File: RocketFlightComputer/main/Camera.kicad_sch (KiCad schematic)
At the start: 1 part

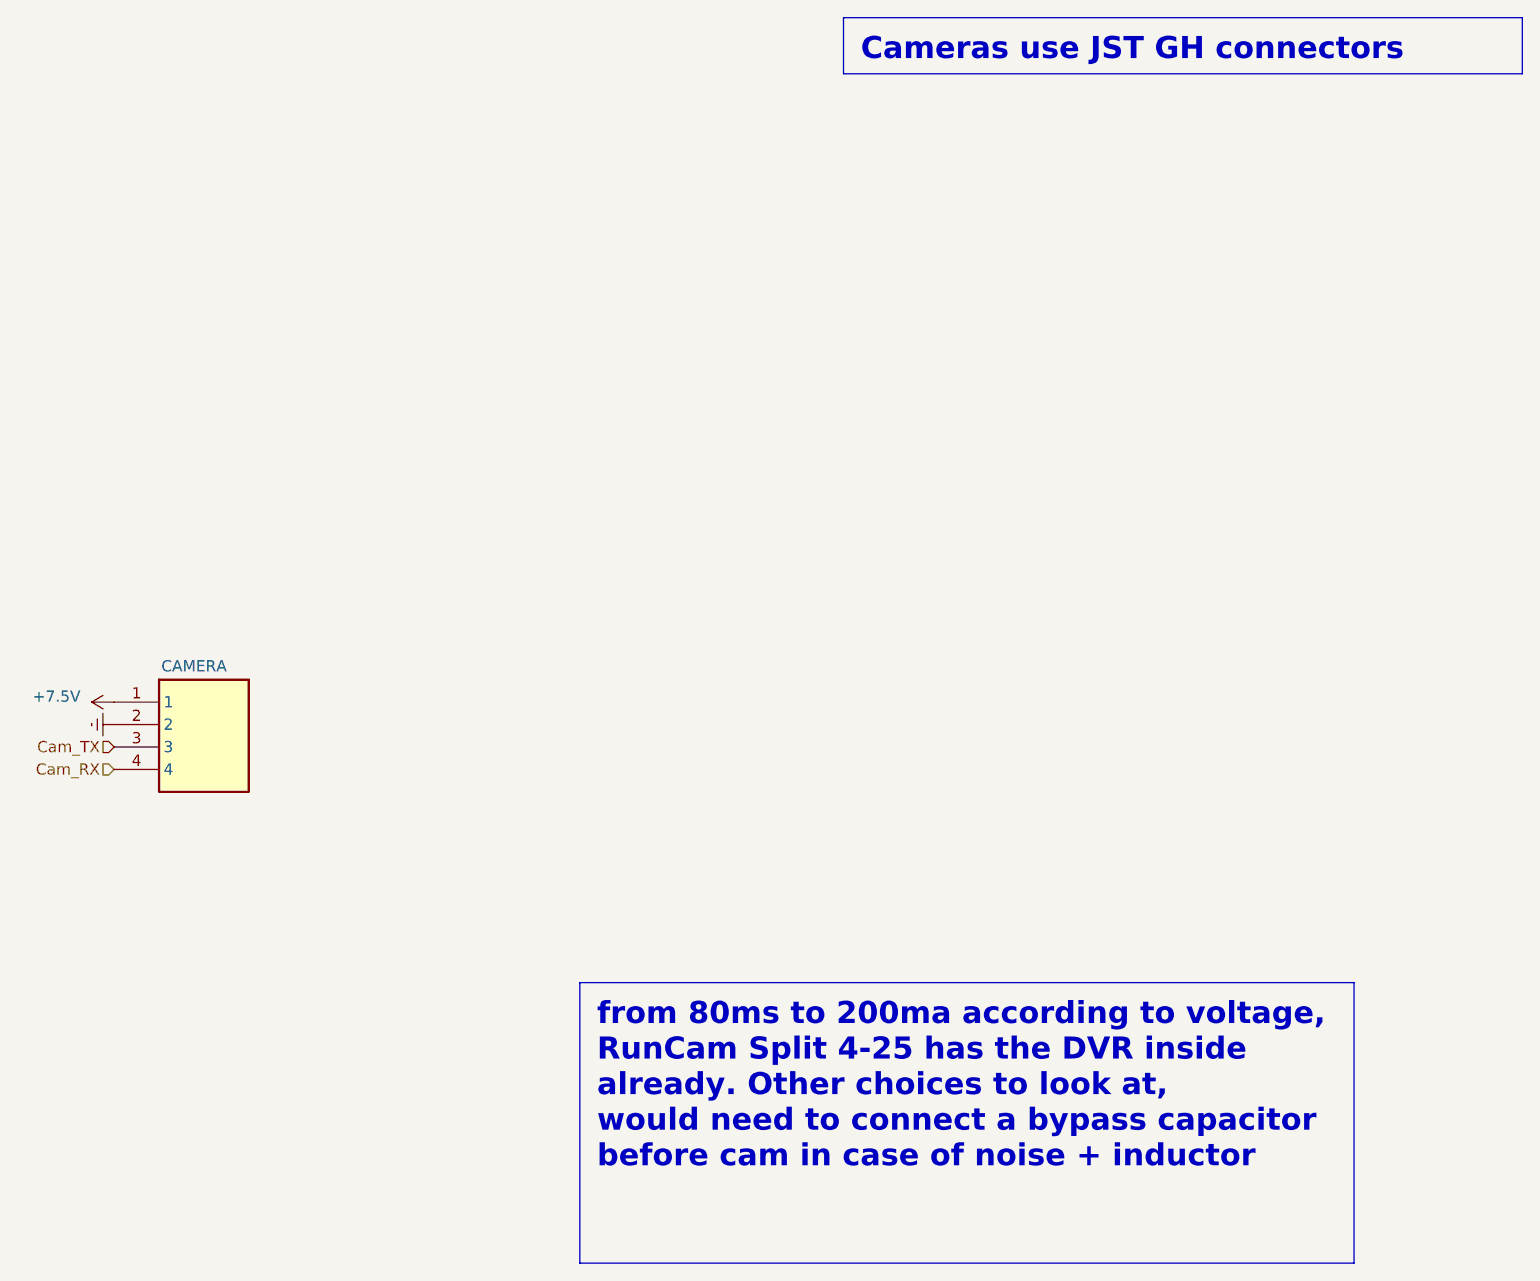
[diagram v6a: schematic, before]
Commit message: Change of winbond flash to other one supported by teensy bootloader since winbond is out of stock
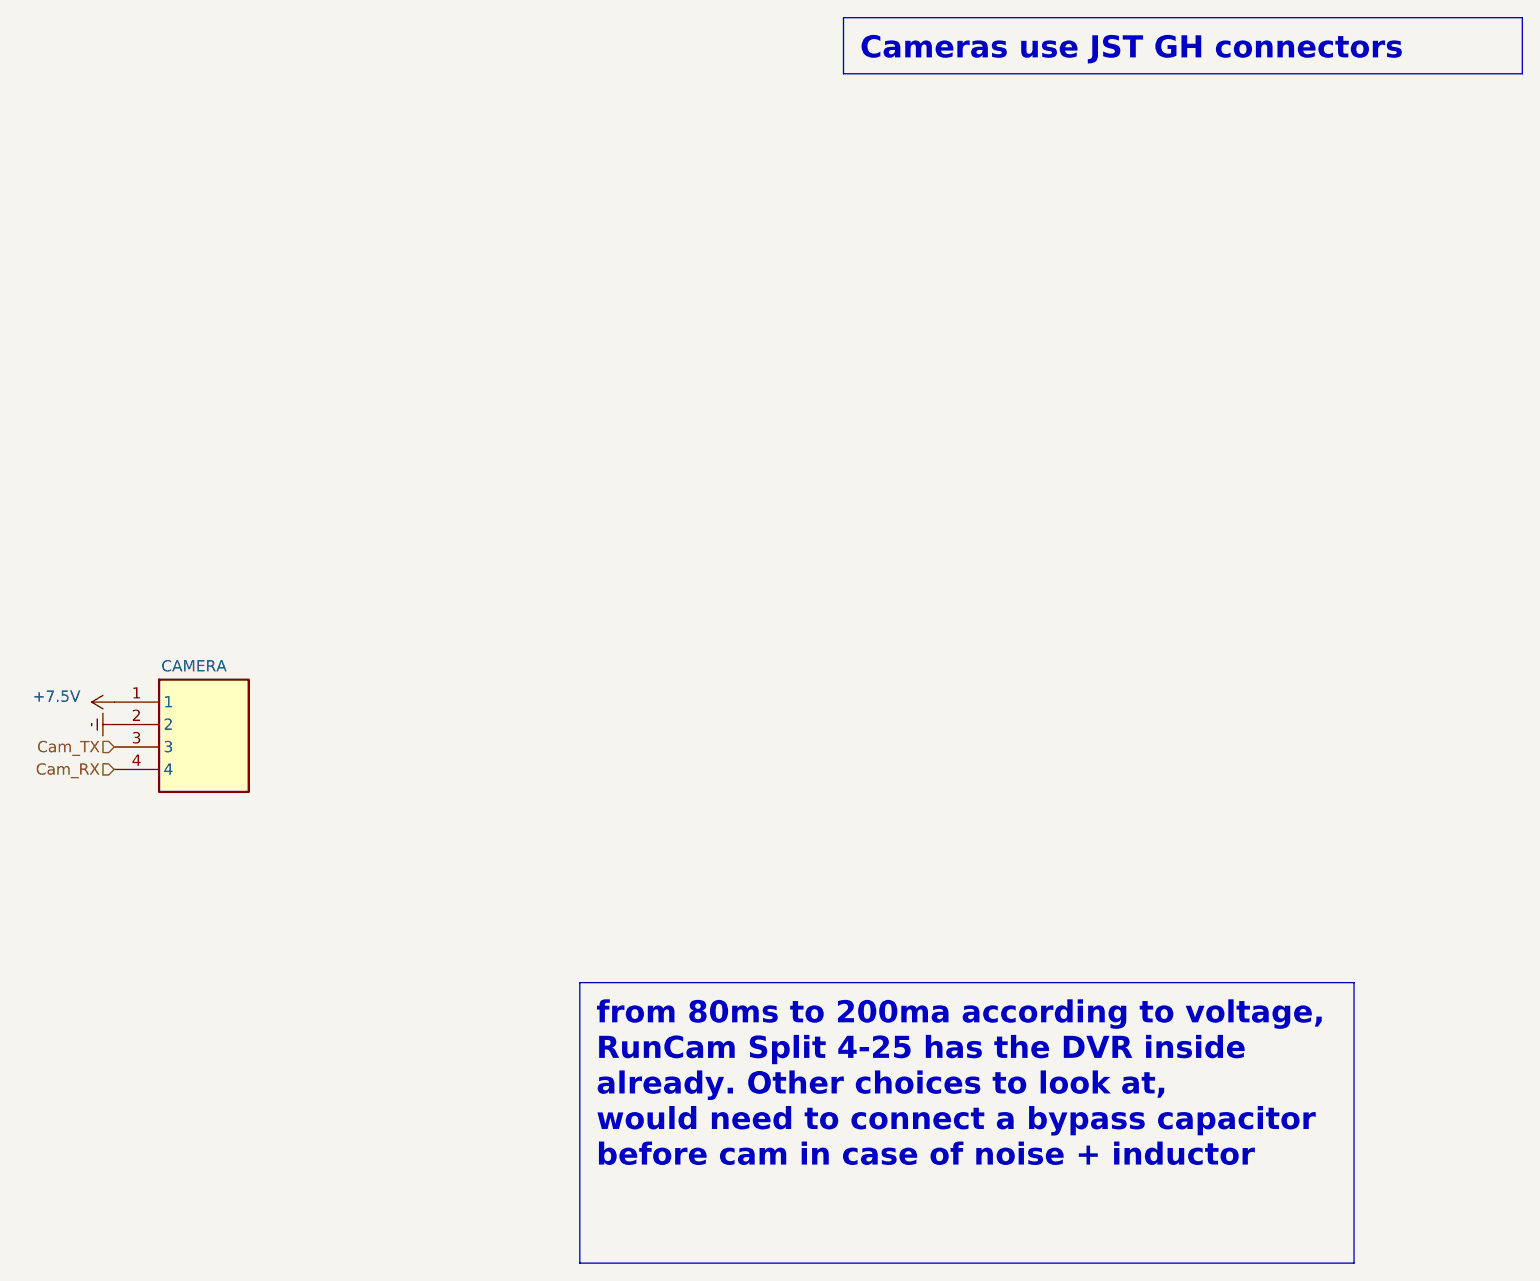
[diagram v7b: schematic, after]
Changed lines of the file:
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@@
 (kicad_sch
-	(version 20231120)
+	(version 20260306)
 	(generator "eeschema")
-	(generator_version "8.0")
+	(generator_version "10.0")
 	(paper "A4")
 	(text_box "from 80ms to 200ma according to voltage, RunCam Split 4-25 has the DVR inside already. Other choices to look at, \nwould need to connect a bypass capacitor before cam in case of noise + inductor"
@@
 		(at 177.165 121.92 0)
 		(size 87.63 31.75)
+		(margins 1.875 1.875 1.875 1.875)
 		(stroke
 			(width 0)
@@
 		(at 207.01 12.7 0)
 		(size 76.835 6.35)
+		(margins 1.875 1.875 1.875 1.875)
 		(stroke
 			(width 0)
@@
 		(shape input)
 		(at 124.46 95.25 180)
-		(fields_autoplaced yes)
 		(effects
 			(font
@@
 		(shape input)
 		(at 124.46 97.79 180)
-		(fields_autoplaced yes)
 		(effects
 			(font
@@
 		(at 124.46 90.17 90)
 		(unit 1)
+		(body_style 1)
 		(exclude_from_sim no)
 		(in_bom yes)
 		(on_board yes)
+		(in_pos_files yes)
 		(dnp no)
 		(property "Reference" "#PWR0143"
 			(at 128.27 90.17 0)
-			(effects
-				(font
-					(size 1.27 1.27)
-				)
-				(hide yes)
+			(hide yes)
+			(show_name no)
+			(do_not_autoplace no)
+			(effects
+				(font
+					(size 1.27 1.27)
+				)
 			)
 		)
 		(property "Value" "+7.5V"
 			(at 120.65 89.535 90)
+			(show_name no)
+			(do_not_autoplace no)
 			(effects
 				(font
@@
 		(property "Footprint" ""
 			(at 124.46 90.17 0)
-			(effects
-				(font
-					(size 1.27 1.27)
-				)
-				(hide yes)
+			(hide yes)
+			(show_name no)
+			(do_not_autoplace no)
+			(effects
+				(font
+					(size 1.27 1.27)
+				)
 			)
 		)
 		(property "Datasheet" ""
 			(at 124.46 90.17 0)
-			(effects
-				(font
-					(size 1.27 1.27)
-				)
-				(hide yes)
+			(hide yes)
+			(show_name no)
+			(do_not_autoplace no)
+			(effects
+				(font
+					(size 1.27 1.27)
+				)
 			)
 		)
 		(property "Description" ""
 			(at 124.46 90.17 0)
-			(effects
-				(font
-					(size 1.27 1.27)
-				)
-				(hide yes)
+			(hide yes)
+			(show_name no)
+			(do_not_autoplace no)
+			(effects
+				(font
+					(size 1.27 1.27)
+				)
 			)
 		)
@@
 		(at 124.46 90.17 0)
 		(unit 1)
+		(body_style 1)
 		(exclude_from_sim no)
 		(in_bom yes)
 		(on_board yes)
+		(in_pos_files yes)
 		(dnp no)
 		(property "Reference" "S4B-PH-K-S_LF__SN_2"
 			(at 130.048 85.852 0)
+			(hide yes)
+			(show_name no)
+			(do_not_autoplace no)
 			(effects
 				(font
@@
 				)
 				(justify left)
-				(hide yes)
 			)
 		)
 		(property "Value" "CAMERA"
 			(at 129.794 86.106 0)
+			(show_name no)
+			(do_not_autoplace no)
 			(effects
 				(font
@@
 		(property "Footprint" "Connector_JST:JST_GH_BM04B-GHS-TBT_1x04-1MP_P1.25mm_Vertical"
 			(at 140.97 185.09 0)
-			(effects
-				(font
-					(size 1.27 1.27)
-				)
-				(justify left top)
-				(hide yes)
+			(hide yes)
+			(show_name no)
+			(do_not_autoplace no)
+			(effects
+				(font
+					(size 1.27 1.27)
+				)
+				(justify left top)
 			)
 		)
 		(property "Datasheet" "https://datasheet.lcsc.com/szlcsc/JST-Sales-America-PHsocket-1-4P-Curved-needle-pitch2mm_C157926.pdf"
 			(at 140.97 285.09 0)
-			(effects
-				(font
-					(size 1.27 1.27)
-				)
-				(justify left top)
-				(hide yes)
+			(hide yes)
+			(show_name no)
+			(do_not_autoplace no)
+			(effects
+				(font
+					(size 1.27 1.27)
+				)
+				(justify left top)
 			)
 		)
 		(property "Description" "CONN HEADER R/A 4POS 2MM"
 			(at 124.46 90.17 0)
-			(effects
-				(font
-					(size 1.27 1.27)
-				)
-				(hide yes)
+			(hide yes)
+			(show_name no)
+			(do_not_autoplace no)
+			(effects
+				(font
+					(size 1.27 1.27)
+				)
 			)
 		)
 		(property "Height" "4.8"
 			(at 140.97 485.09 0)
-			(effects
-				(font
-					(size 1.27 1.27)
-				)
-				(justify left top)
-				(hide yes)
+			(hide yes)
+			(show_name no)
+			(do_not_autoplace no)
+			(effects
+				(font
+					(size 1.27 1.27)
+				)
+				(justify left top)
 			)
 		)
 		(property "Mouser Part Number" "306-BM04BGHSTBTLFSNN"
 			(at 140.97 585.09 0)
-			(effects
-				(font
-					(size 1.27 1.27)
-				)
-				(justify left top)
-				(hide yes)
+			(hide yes)
+			(show_name no)
+			(do_not_autoplace no)
+			(effects
+				(font
+					(size 1.27 1.27)
+				)
+				(justify left top)
 			)
 		)
 		(property "Mouser Price/Stock" "https://www.mouser.co.uk/ProductDetail/JST-Commercial/S4B-PH-K-SLFSN?qs=QpmGXVUTftEGA16rwNx4xw%3D%3D"
 			(at 140.97 685.09 0)
-			(effects
-				(font
-					(size 1.27 1.27)
-				)
-				(justify left top)
-				(hide yes)
+			(hide yes)
+			(show_name no)
+			(do_not_autoplace no)
+			(effects
+				(font
+					(size 1.27 1.27)
+				)
+				(justify left top)
 			)
 		)
 		(property "Manufacturer_Name" "JST (JAPAN SOLDERLESS TERMINALS)"
 			(at 140.97 785.09 0)
-			(effects
-				(font
-					(size 1.27 1.27)
-				)
-				(justify left top)
-				(hide yes)
+			(hide yes)
+			(show_name no)
+			(do_not_autoplace no)
+			(effects
+				(font
+					(size 1.27 1.27)
+				)
+				(justify left top)
 			)
 		)
 		(property "Manufacturer_Part_Number" "S4B-PH-K-S(LF)(SN)"
 			(at 140.97 885.09 0)
-			(effects
-				(font
-					(size 1.27 1.27)
-				)
-				(justify left top)
-				(hide yes)
+			(hide yes)
+			(show_name no)
+			(do_not_autoplace no)
+			(effects
+				(font
+					(size 1.27 1.27)
+				)
+				(justify left top)
 			)
 		)
 		(property "LCSC" "C161692"
 			(at 124.46 90.17 0)
-			(effects
-				(font
-					(size 1.27 1.27)
-				)
-				(hide yes)
+			(hide yes)
+			(show_name no)
+			(do_not_autoplace no)
+			(effects
+				(font
+					(size 1.27 1.27)
+				)
 			)
 		)
@@
 		(at 124.46 92.71 270)
 		(unit 1)
+		(body_style 1)
 		(exclude_from_sim no)
 		(in_bom yes)
 		(on_board yes)
+		(in_pos_files yes)
 		(dnp no)
 		(fields_autoplaced yes)
 		(property "Reference" "#PWR0144"
 			(at 118.11 92.71 0)
-			(effects
-				(font
-					(size 1.27 1.27)
-				)
-				(hide yes)
+			(hide yes)
+			(show_name no)
+			(do_not_autoplace no)
+			(effects
+				(font
+					(size 1.27 1.27)
+				)
 			)
 		)
 		(property "Value" "GNDREF"
 			(at 120.65 92.075 90)
+			(hide yes)
+			(show_name no)
+			(do_not_autoplace no)
 			(effects
 				(font
@@
 				)
 				(justify right)
-				(hide yes)
 			)
 		)
 		(property "Footprint" ""
 			(at 124.46 92.71 0)
-			(effects
-				(font
-					(size 1.27 1.27)
-				)
-				(hide yes)
+			(hide yes)
+			(show_name no)
+			(do_not_autoplace no)
+			(effects
+				(font
+					(size 1.27 1.27)
+				)
 			)
 		)
 		(property "Datasheet" ""
 			(at 124.46 92.71 0)
-			(effects
-				(font
-					(size 1.27 1.27)
-				)
-				(hide yes)
+			(hide yes)
+			(show_name no)
+			(do_not_autoplace no)
+			(effects
+				(font
+					(size 1.27 1.27)
+				)
 			)
 		)
 		(property "Description" ""
 			(at 124.46 92.71 0)
-			(effects
-				(font
-					(size 1.27 1.27)
-				)
-				(hide yes)
-			)
-		)
+			(hide yes)
+			(show_name no)
+			(do_not_autoplace no)
+			(effects
+				(font
+					(size 1.27 1.27)
+				)
+			)
+		)

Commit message: REVA board?
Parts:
- renumbered S4B-PH-K-S_LF__SN_2 to JST-GH-2
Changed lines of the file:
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@@
 		(in_pos_files yes)
 		(dnp no)
-		(property "Reference" "S4B-PH-K-S_LF__SN_2"
+		(property "Reference" "JST-GH-2"
 			(at 130.048 85.852 0)
 			(hide yes)
@@
 			(project "main"
 				(path "/27195d1d-92b2-40df-ada5-3b20841577e7/e516ca7f-4a7c-4d6f-878d-eb9fde5d9c52"
-					(reference "S4B-PH-K-S_LF__SN_2")
+					(reference "JST-GH-2")
 					(unit 1)
 				)
